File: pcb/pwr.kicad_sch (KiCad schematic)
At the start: 3 parts, among them J10 Barrel_Jack_Switch, J11 Screw_Terminal_01x02, Q9 Q_PMOS_GDS

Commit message: new layout with usb
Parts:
- removed Q9: Q_PMOS_GDS, Package_TO_SOT_THT:TO-220-3_Horizontal_TabDown, symbol Device:Q_PMOS_GDS
- added C21, C22: 100nF, Capacitor_SMD:C_0805_2012Metric_Pad1.18x1.45mm_HandSolder, symbol Device:C_Small
- added C23, C24: 10uF, Capacitor_SMD:C_0805_2012Metric_Pad1.18x1.45mm_HandSolder, symbol Device:C_Small
- added D15: RX_Led Blue, LED_SMD:LED_0805_2012Metric_Pad1.15x1.40mm_HandSolder, symbol Device:LED
- added D16: TX_Led Green, LED_SMD:LED_0805_2012Metric_Pad1.15x1.40mm_HandSolder, symbol Device:LED
- added D17: MBR130HW, Diode_SMD:D_SOD-123, symbol Device:D_Schottky_Small
- added D18: PWR_Led, LED_SMD:LED_0805_2012Metric_Pad1.15x1.40mm_HandSolder, symbol Device:LED
- added J15: USB_B, Connector_USB:USB_B_OST_USB-B1HSxx_Horizontal, symbol Connector:USB_B
- added R66, R67, R68: 1k, Resistor_SMD:R_0805_2012Metric_Pad1.20x1.40mm_HandSolder, symbol Device:R_Small
- added U12: FT232RL, Package_SO:SSOP-28_5.3x10.2mm_P0.65mm, symbol Interface_USB:FT232RL
- added U13: NCP1117-5.0_SOT223, Package_TO_SOT_SMD:SOT-223-3_TabPin2, symbol Regulator_Linear:NCP1117-5.0_SOT223
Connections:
- net +5V: now also C24.1, D15.2 (A), D16.2 (A), D17.1 (K), R68.1, U12.20 (VCC), U12.4 (VCCIO), U13.2 (VO)
- net GND: now also C22.2, C23.2, C24.2, D18.1 (K), J15.4 (GND), J15.5 (Shield), U12.18 (GND), U12.21 (GND), U12.25 (AGND), U12.26 (TEST), U12.7 (GND), U13.1 (GND)
- net Vin: now reaches J10.1, J11.1 (Pin_1)
- net Vin: now also C23.1, U13.3 (VI)
- new net: D15.1 (K), R66.1
- new net: R66.2, U12.23 (CBUS0)
- new net: J15.3 (D+), U12.15 (USBD+)
- new net: J15.2 (D-), U12.16 (USBD-)
- new net: C21.1, U12.2 (DTR)
- new net: R67.2, U12.22 (CBUS1)
- new net: D16.1 (K), R67.1
- new net: D18.2 (A), R68.2
- new net +3.3V: C22.1, U12.17 (3V3OUT)
- new net RXD: U12.1 (TXD)
- new net TXD: U12.5 (RXD)
- new net VUSB: D17.2 (A), J15.1 (VBUS)
- new net reset: C21.2
- no-connect marks 0 -> 11

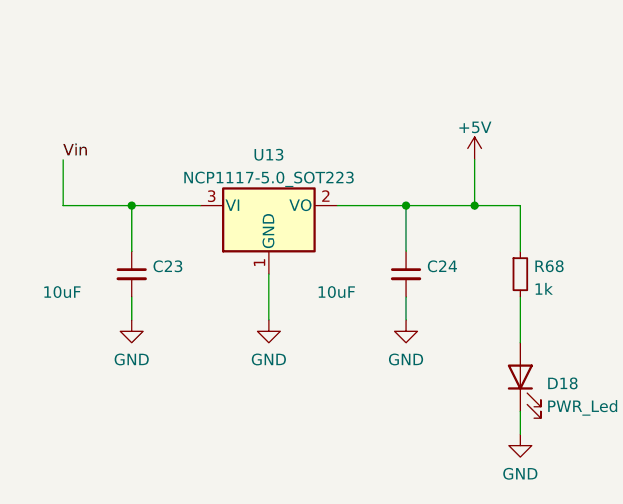
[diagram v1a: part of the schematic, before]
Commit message: pulldown to signals
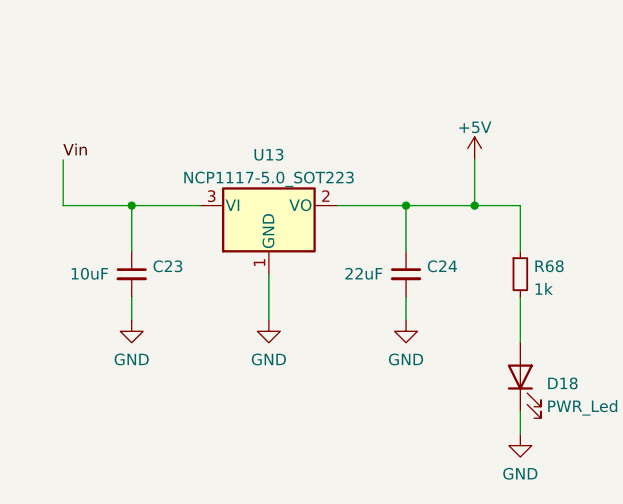
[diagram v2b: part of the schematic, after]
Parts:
- C24: value 10uF -> 22uF
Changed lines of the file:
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@@
       (effects (font (size 1.27 1.27)) (justify left))
     )
-    (property "Value" "10uF" (id 1) (at 81.534 136.652 0)
+    (property "Value" "22uF" (id 1) (at 84.582 134.62 0)
       (effects (font (size 1.27 1.27)) (justify left))
     )
@@
       (effects (font (size 1.27 1.27)) (justify left))
     )
-    (property "Value" "10uF" (id 1) (at 51.054 136.652 0)
-      (effects (font (size 1.27 1.27)) (justify left))
-    )
+    (property "Value" "10uF" (id 1) (at 54.102 134.62 0)
+      (effects (font (size 1.27 1.27)) (justify left))
+    )
